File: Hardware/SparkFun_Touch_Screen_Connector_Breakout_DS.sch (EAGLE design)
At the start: 3 parts

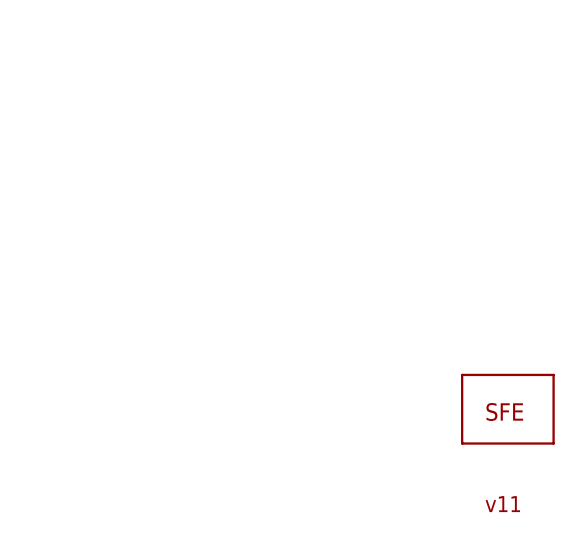
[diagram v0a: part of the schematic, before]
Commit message: added board fiducials
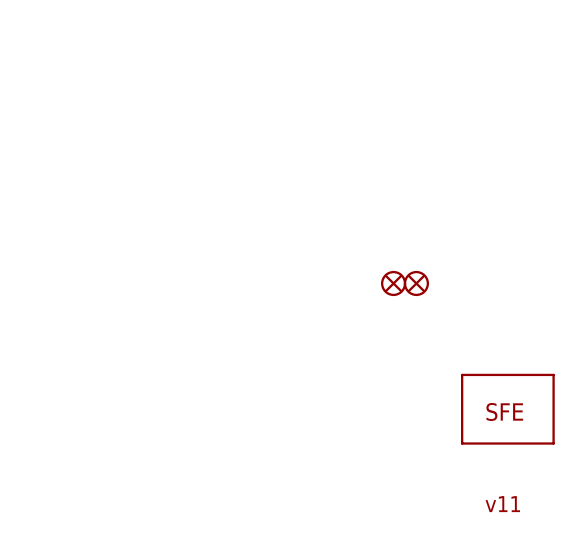
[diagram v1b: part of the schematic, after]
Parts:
- added FID1, FID2: FIDUCIAL1X2, SparkFun-Aesthetics:FIDUCIAL1X2
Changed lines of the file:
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@@
 <?xml version="1.0" encoding="utf-8"?>
 <!DOCTYPE eagle SYSTEM "eagle.dtd">
-<eagle version="7.2.0">
+<eagle version="7.5.0">
 <drawing>
 <settings>
@@
 <layer number="54" name="bGND_GNDA" color="1" fill="9" visible="no" active="no"/>
 <layer number="56" name="wert" color="7" fill="1" visible="no" active="no"/>
+<layer number="57" name="tCAD" color="7" fill="1" visible="no" active="no"/>
+<layer number="59" name="tCarbon" color="7" fill="1" visible="no" active="no"/>
+<layer number="60" name="bCarbon" color="7" fill="1" visible="no" active="no"/>
+<layer number="90" name="Modules" color="5" fill="1" visible="yes" active="yes"/>
 <layer number="91" name="Nets" color="2" fill="1" visible="yes" active="yes"/>
 <layer number="92" name="Busses" color="1" fill="1" visible="yes" active="yes"/>
@@
 <layer number="97" name="Info" color="7" fill="1" visible="yes" active="yes"/>
 <layer number="98" name="Guide" color="6" fill="1" visible="yes" active="yes"/>
+<layer number="99" name="SpiceOrder" color="7" fill="1" visible="no" active="no"/>
 <layer number="100" name="Muster" color="7" fill="1" visible="no" active="no"/>
 <layer number="101" name="Patch_Top" color="12" fill="4" visible="yes" active="yes"/>
 <layer number="102" name="Vscore" color="7" fill="1" visible="yes" active="yes"/>
+<layer number="103" name="tMap" color="7" fill="1" visible="yes" active="yes"/>
 <layer number="104" name="Name" color="7" fill="1" visible="yes" active="yes"/>
+<layer number="105" name="tPlate" color="7" fill="1" visible="yes" active="yes"/>
+<layer number="106" name="bPlate" color="7" fill="1" visible="yes" active="yes"/>
+<layer number="107" name="Crop" color="7" fill="1" visible="yes" active="yes"/>
+<layer number="108" name="tplace-old" color="10" fill="1" visible="yes" active="yes"/>
+<layer number="109" name="ref-old" color="11" fill="1" visible="yes" active="yes"/>
+<layer number="110" name="fp0" color="7" fill="1" visible="yes" active="yes"/>
+<layer number="111" name="LPC17xx" color="7" fill="1" visible="yes" active="yes"/>
+<layer number="112" name="tSilk" color="7" fill="1" visible="yes" active="yes"/>
+<layer number="113" name="IDFDebug" color="4" fill="1" visible="yes" active="yes"/>
 <layer number="116" name="Patch_BOT" color="9" fill="4" visible="yes" active="yes"/>
 <layer number="121" name="_tsilk" color="7" fill="1" visible="yes" active="yes"/>
 <layer number="122" name="_bsilk" color="7" fill="1" visible="yes" active="yes"/>
+<layer number="123" name="tTestmark" color="7" fill="1" visible="yes" active="yes"/>
+<layer number="124" name="bTestmark" color="7" fill="1" visible="yes" active="yes"/>
+<layer number="125" name="_tNames" color="7" fill="1" visible="yes" active="yes"/>
+<layer number="126" name="_bNames" color="7" fill="1" visible="yes" active="yes"/>
+<layer number="127" name="_tValues" color="7" fill="1" visible="yes" active="yes"/>
+<layer number="128" name="_bValues" color="7" fill="1" visible="yes" active="yes"/>
+<layer number="129" name="Mask" color="7" fill="1" visible="yes" active="yes"/>
+<layer number="131" name="tAdjust" color="7" fill="1" visible="yes" active="yes"/>
+<layer number="132" name="bAdjust" color="7" fill="1" visible="yes" active="yes"/>
+<layer number="144" name="Drill_legend" color="7" fill="1" visible="yes" active="yes"/>
+<layer number="150" name="Notes" color="7" fill="1" visible="yes" active="yes"/>
 <layer number="151" name="HeatSink" color="7" fill="1" visible="yes" active="yes"/>
+<layer number="152" name="_bDocu" color="7" fill="1" visible="yes" active="yes"/>
+<layer number="153" name="FabDoc1" color="7" fill="1" visible="yes" active="yes"/>
+<layer number="154" name="FabDoc2" color="7" fill="1" visible="yes" active="yes"/>
+<layer number="155" name="FabDoc3" color="7" fill="1" visible="yes" active="yes"/>
+<layer number="199" name="Contour" color="7" fill="1" visible="yes" active="yes"/>
 <layer number="200" name="200bmp" color="1" fill="10" visible="no" active="no"/>
 <layer number="201" name="201bmp" color="2" fill="1" visible="no" active="no"/>
 <layer number="202" name="202bmp" color="3" fill="1" visible="no" active="no"/>
+<layer number="203" name="203bmp" color="4" fill="10" visible="yes" active="yes"/>
+<layer number="204" name="204bmp" color="5" fill="10" visible="yes" active="yes"/>
+<layer number="205" name="205bmp" color="6" fill="10" visible="yes" active="yes"/>
+<layer number="206" name="206bmp" color="7" fill="10" visible="yes" active="yes"/>
+<layer number="207" name="207bmp" color="8" fill="10" visible="yes" active="yes"/>
+<layer number="208" name="208bmp" color="9" fill="10" visible="yes" active="yes"/>
+<layer number="209" name="209bmp" color="7" fill="1" visible="yes" active="yes"/>
+<layer number="210" name="210bmp" color="7" fill="1" visible="yes" active="yes"/>
+<layer number="211" name="211bmp" color="7" fill="1" visible="yes" active="yes"/>
+<layer number="212" name="212bmp" color="7" fill="1" visible="yes" active="yes"/>
+<layer number="213" name="213bmp" color="7" fill="1" visible="yes" active="yes"/>
+<layer number="214" name="214bmp" color="7" fill="1" visible="yes" active="yes"/>
+<layer number="215" name="215bmp" color="7" fill="1" visible="yes" active="yes"/>
+<layer number="216" name="216bmp" color="7" fill="1" visible="yes" active="yes"/>
+<layer number="217" name="217bmp" color="18" fill="1" visible="no" active="no"/>
+<layer number="218" name="218bmp" color="19" fill="1" visible="no" active="no"/>
+<layer number="219" name="219bmp" color="20" fill="1" visible="no" active="no"/>
+<layer number="220" name="220bmp" color="21" fill="1" visible="no" active="no"/>
+<layer number="221" name="221bmp" color="22" fill="1" visible="no" active="no"/>
+<layer number="222" name="222bmp" color="23" fill="1" visible="no" active="no"/>
+<layer number="223" name="223bmp" color="24" fill="1" visible="no" active="no"/>
+<layer number="224" name="224bmp" color="25" fill="1" visible="no" active="no"/>
+<layer number="225" name="225bmp" color="7" fill="1" visible="yes" active="yes"/>
+<layer number="226" name="226bmp" color="7" fill="1" visible="yes" active="yes"/>
+<layer number="227" name="227bmp" color="7" fill="1" visible="yes" active="yes"/>
+<layer number="228" name="228bmp" color="7" fill="1" visible="yes" active="yes"/>
+<layer number="229" name="229bmp" color="7" fill="1" visible="yes" active="yes"/>
+<layer number="230" name="230bmp" color="7" fill="1" visible="yes" active="yes"/>
+<layer number="231" name="231bmp" color="7" fill="1" visible="yes" active="yes"/>
+<layer number="248" name="Housing" color="7" fill="1" visible="yes" active="yes"/>
+<layer number="249" name="Edge" color="7" fill="1" visible="yes" active="yes"/>
 <layer number="250" name="Descript" color="3" fill="1" visible="no" active="no"/>
 <layer number="251" name="SMDround" color="12" fill="11" visible="no" active="no"/>
 <layer number="254" name="cooling" color="7" fill="1" visible="yes" active="yes"/>
+<layer number="255" name="routoute" color="7" fill="1" visible="yes" active="yes"/>
 </layers>
 <schematic xreflabel="%F%N/%S" xrefpart="/%S">
@@
 <part name="U$2" library="SparkFun" deviceset="LOGO-SFE" device="SK"/>
 <part name="U$1" library="SparkFun" deviceset="DS_TOUCH_CONNECTOR" device=""/>
+<part name="FID1" library="SparkFun-Aesthetics" deviceset="FIDUCIAL" device="1X2"/>
+<part name="FID2" library="SparkFun-Aesthetics" deviceset="FIDUCIAL" device="1X2"/>
 </parts>
 <sheets>
@@
 <instance part="U$2" gate="G$1" x="241.3" y="17.78"/>
 <instance part="U$1" gate="G$1" x="106.68" y="104.14"/>
+<instance part="FID1" gate="G$1" x="231.14" y="33.02"/>
+<instance part="FID2" gate="G$1" x="233.68" y="33.02"/>
 </instances>
 <busses>
